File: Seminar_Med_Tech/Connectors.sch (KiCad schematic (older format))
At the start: 14 parts, among them J2 CONN_01X10, J3 CONN_02X10, J5 CONN_02X10

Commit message: update anno
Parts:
- gave numbers to parts that had none: 4
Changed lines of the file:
@@
 $EndComp
 $Comp
-L GND #PWR01
+L GND #PWR4
 U 1 1 593AE084
 P 7225 6000
-F 0 "#PWR01" H 7225 5750 50  0001 C CNN
+F 0 "#PWR4" H 7225 5750 50  0001 C CNN
 F 1 "GND" H 7225 5850 50  0000 C CNN
 F 2 "" H 7225 6000 50  0001 C CNN
@@
 $EndComp
 $Comp
-L GND #PWR02
+L GND #PWR2
 U 1 1 593AE114
 P 3675 5000
-F 0 "#PWR02" H 3675 4750 50  0001 C CNN
+F 0 "#PWR2" H 3675 4750 50  0001 C CNN
 F 1 "GND" H 3675 4850 50  0000 C CNN
 F 2 "" H 3675 5000 50  0001 C CNN
@@
 $EndComp
 $Comp
-L GND #PWR03
+L GND #PWR6
 U 1 1 593AE149
 P 9375 3700
-F 0 "#PWR03" H 9375 3450 50  0001 C CNN
+F 0 "#PWR6" H 9375 3450 50  0001 C CNN
 F 1 "GND" H 9375 3550 50  0000 C CNN
 F 2 "" H 9375 3700 50  0001 C CNN
@@
 SPI_CS2
 $Comp
-L GND #PWR04
+L GND #PWR5
 U 1 1 593E72B3
 P 9200 5600
-F 0 "#PWR04" H 9200 5350 50  0001 C CNN
+F 0 "#PWR5" H 9200 5350 50  0001 C CNN
 F 1 "GND" H 9200 5450 50  0000 C CNN
 F 2 "" H 9200 5600 50  0001 C CNN
@@
 $EndComp
 $Comp
-L GND #PWR05
+L GND #PWR3
 U 1 1 593E9316
 P 4700 4150
-F 0 "#PWR05" H 4700 3900 50  0001 C CNN
+F 0 "#PWR3" H 4700 3900 50  0001 C CNN
 F 1 "GND" H 4700 4000 50  0000 C CNN
 F 2 "" H 4700 4150 50  0001 C CNN
@@
 NoConn ~ 3850 6225
 $Comp
-L Jumper JP?
+L Jumper JP2
 U 1 1 5947B7A9
 P 1950 3550
-F 0 "JP?" H 1950 3700 50  0000 C CNN
+F 0 "JP2" H 1950 3700 50  0000 C CNN
 F 1 "Jumper" H 1950 3470 50  0000 C CNN
 F 2 "jumper:Jumper1x2" H 1950 3550 50  0001 C CNN
@@
 $EndComp
 $Comp
-L TEST_1P TP?
+L TEST_1P TP8
 U 1 1 5947B7AF
 P 1525 3550
-F 0 "TP?" H 1525 3820 50  0000 C CNN
+F 0 "TP8" H 1525 3820 50  0000 C CNN
 F 1 "TEST" H 1525 3750 50  0000 C CNN
 F 2 "Measurement_Points:Test_Point_Keystone_5000-5004_Miniature" H 1725 3550 50  0001 C CNN
@@
 $EndComp
 $Comp
-L C C?
+L C C33
 U 1 1 5947B7B5
 P 1300 3900
-F 0 "C?" H 1325 4000 50  0000 L CNN
+F 0 "C33" H 1325 4000 50  0000 L CNN
 F 1 "0.1uF" H 1325 3800 50  0000 L CNN
 F 2 "Capacitors_SMD:C_1206_HandSoldering" H 1338 3750 50  0001 C CNN
@@
 $EndComp
 $Comp
-L C C?
+L C C27
 U 1 1 5947B7BB
 P 925 3900
-F 0 "C?" H 950 4000 50  0000 L CNN
+F 0 "C27" H 950 4000 50  0000 L CNN
 F 1 "100uF" H 950 3800 50  0000 L CNN
 F 2 "Capacitors_SMD:C_1206_HandSoldering" H 963 3750 50  0001 C CNN
@@
 $EndComp
 $Comp
-L GND #PWR?
+L GND #PWR1
 U 1 1 5947B7C1
 P 1100 4150
-F 0 "#PWR?" H 1100 3900 50  0001 C CNN
+F 0 "#PWR1" H 1100 3900 50  0001 C CNN
 F 1 "GND" H 1100 4000 50  0000 C CNN
 F 2 "" H 1100 4150 50  0001 C CNN

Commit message: hi
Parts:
- TP7, TP8: footprint Measurement_Points:Test_Point_Keystone_5000-5004_Miniature -> Measurement_Points:Measurement_Point_Round-SMD-Pad_Small
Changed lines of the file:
@@
 $EndComp
 $Comp
-L GND #PWR4
+L GND #PWR01
 U 1 1 593AE084
 P 7225 6000
-F 0 "#PWR4" H 7225 5750 50  0001 C CNN
+F 0 "#PWR01" H 7225 5750 50  0001 C CNN
 F 1 "GND" H 7225 5850 50  0000 C CNN
 F 2 "" H 7225 6000 50  0001 C CNN
@@
 $EndComp
 $Comp
-L GND #PWR2
+L GND #PWR02
 U 1 1 593AE114
 P 3675 5000
-F 0 "#PWR2" H 3675 4750 50  0001 C CNN
+F 0 "#PWR02" H 3675 4750 50  0001 C CNN
 F 1 "GND" H 3675 4850 50  0000 C CNN
 F 2 "" H 3675 5000 50  0001 C CNN
@@
 $EndComp
 $Comp
-L GND #PWR6
+L GND #PWR03
 U 1 1 593AE149
 P 9375 3700
-F 0 "#PWR6" H 9375 3450 50  0001 C CNN
+F 0 "#PWR03" H 9375 3450 50  0001 C CNN
 F 1 "GND" H 9375 3550 50  0000 C CNN
 F 2 "" H 9375 3700 50  0001 C CNN
@@
 SPI_CS2
 $Comp
-L GND #PWR5
+L GND #PWR04
 U 1 1 593E72B3
 P 9200 5600
-F 0 "#PWR5" H 9200 5350 50  0001 C CNN
+F 0 "#PWR04" H 9200 5350 50  0001 C CNN
 F 1 "GND" H 9200 5450 50  0000 C CNN
 F 2 "" H 9200 5600 50  0001 C CNN
@@
 F 0 "TP7" H 4275 3820 50  0000 C CNN
 F 1 "TEST" H 4275 3750 50  0000 C CNN
-F 2 "Measurement_Points:Test_Point_Keystone_5000-5004_Miniature" H 4475 3550 50  0001 C CNN
+F 2 "Measurement_Points:Measurement_Point_Round-SMD-Pad_Small" H 4475 3550 50  0001 C CNN
 F 3 "" H 4475 3550 50  0001 C CNN
 	1    4275 3550
@@
 $EndComp
 $Comp
-L GND #PWR3
+L GND #PWR05
 U 1 1 593E9316
 P 4700 4150
-F 0 "#PWR3" H 4700 3900 50  0001 C CNN
+F 0 "#PWR05" H 4700 3900 50  0001 C CNN
 F 1 "GND" H 4700 4000 50  0000 C CNN
 F 2 "" H 4700 4150 50  0001 C CNN
@@
 F 0 "TP8" H 1525 3820 50  0000 C CNN
 F 1 "TEST" H 1525 3750 50  0000 C CNN
-F 2 "Measurement_Points:Test_Point_Keystone_5000-5004_Miniature" H 1725 3550 50  0001 C CNN
+F 2 "Measurement_Points:Measurement_Point_Round-SMD-Pad_Small" H 1725 3550 50  0001 C CNN
 F 3 "" H 1725 3550 50  0001 C CNN
 	1    1525 3550
@@
 $EndComp
 $Comp
-L GND #PWR1
+L GND #PWR06
 U 1 1 5947B7C1
 P 1100 4150
-F 0 "#PWR1" H 1100 3900 50  0001 C CNN
+F 0 "#PWR06" H 1100 3900 50  0001 C CNN
 F 1 "GND" H 1100 4000 50  0000 C CNN
 F 2 "" H 1100 4150 50  0001 C CNN

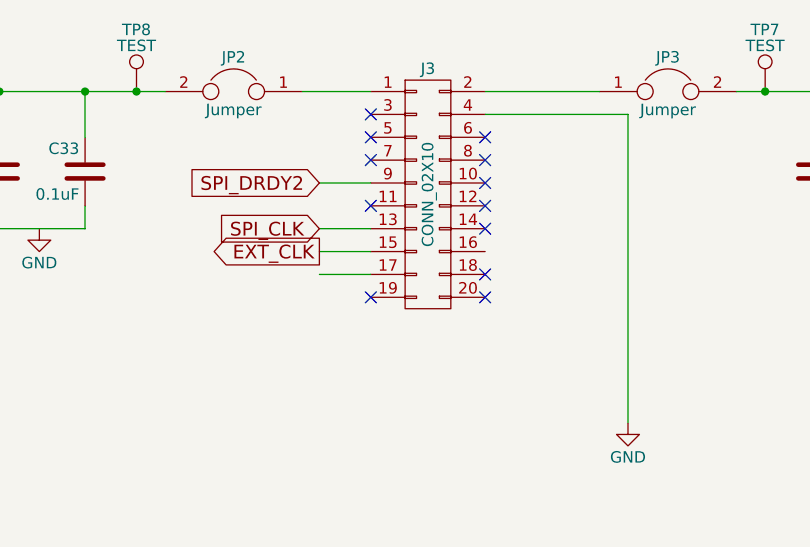
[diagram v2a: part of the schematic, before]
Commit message: Updated Connectors
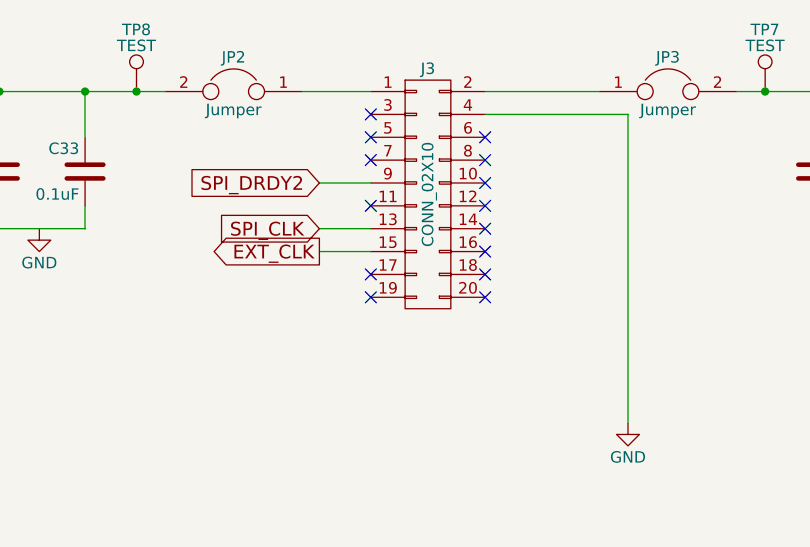
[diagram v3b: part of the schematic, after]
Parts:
- TP7, TP8: footprint Measurement_Points:Measurement_Point_Round-SMD-Pad_Small -> Measurement_Points:Test_Point_Keystone_5000-5004_Miniature
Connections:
- no-connect marks 17 -> 19
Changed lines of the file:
@@
 F 0 "TP7" H 4275 3820 50  0000 C CNN
 F 1 "TEST" H 4275 3750 50  0000 C CNN
-F 2 "Measurement_Points:Measurement_Point_Round-SMD-Pad_Small" H 4475 3550 50  0001 C CNN
+F 2 "Measurement_Points:Test_Point_Keystone_5000-5004_Miniature" H 4475 3550 50  0001 C CNN
 F 3 "" H 4475 3550 50  0001 C CNN
 	1    4275 3550
@@
 Wire Wire Line
 	2550 3950 2325 3950
-Wire Wire Line
-	2325 4350 2550 4350
 $Comp
 L CONN_01X10 J2
@@
 F 0 "TP8" H 1525 3820 50  0000 C CNN
 F 1 "TEST" H 1525 3750 50  0000 C CNN
-F 2 "Measurement_Points:Measurement_Point_Round-SMD-Pad_Small" H 1725 3550 50  0001 C CNN
+F 2 "Measurement_Points:Test_Point_Keystone_5000-5004_Miniature" H 1725 3550 50  0001 C CNN
 F 3 "" H 1725 3550 50  0001 C CNN
 	1    1525 3550
@@
 NoConn ~ 2550 3750
 NoConn ~ 2550 3850
+NoConn ~ 3050 4250
+NoConn ~ 2550 4350
 $EndSCHEMATC

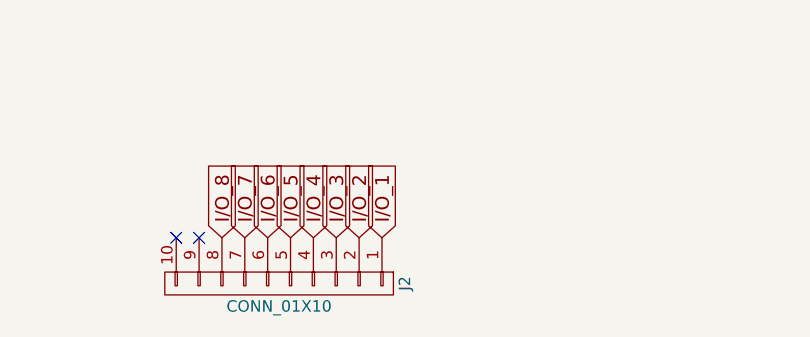
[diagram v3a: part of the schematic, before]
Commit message: Updated Schaltbild and changed BOM
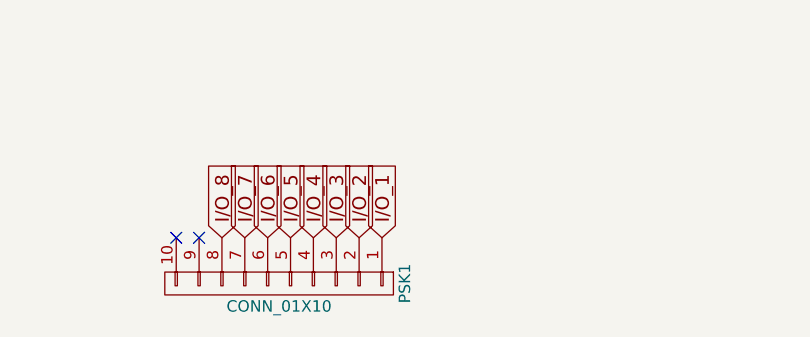
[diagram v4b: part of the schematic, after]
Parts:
- renumbered J2 to PSK1
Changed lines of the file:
@@
 	2550 3950 2325 3950
 $Comp
-L CONN_01X10 J2
+L CONN_01X10 PSK1
 U 1 1 5962D12A
 P 4200 6425
-F 0 "J2" H 4200 6975 50  0000 C CNN
+F 0 "PSK1" H 4200 6975 50  0000 C CNN
 F 1 "CONN_01X10" V 4300 6425 50  0000 C CNN
 F 2 "Pin_Headers:Pin_Header_Straight_1x10_Pitch2.54mm" H 4200 6425 50  0001 C CNN

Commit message: Updated Schaltbild and added LM317 footprint
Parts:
- JP2, JP3: footprint jumper:Jumper1x2 -> Jumper:Jumper1x2
- JP21: footprint jumper:jumper1x3 -> Jumper:jumper1x3
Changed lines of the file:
@@
 F 0 "JP21" H 7275 5650 50  0000 L CNN
 F 1 "Jumper_NC_Dual" H 7225 5850 50  0000 C BNN
-F 2 "jumper:jumper1x3" H 7225 5750 50  0001 C CNN
+F 2 "Jumper:jumper1x3" H 7225 5750 50  0001 C CNN
 F 3 "" H 7225 5750 50  0001 C CNN
 	1    7225 5750
@@
 F 0 "JP3" H 3850 3700 50  0000 C CNN
 F 1 "Jumper" H 3850 3470 50  0000 C CNN
-F 2 "jumper:Jumper1x2" H 3850 3550 50  0001 C CNN
+F 2 "Jumper:Jumper1x2" H 3850 3550 50  0001 C CNN
 F 3 "" H 3850 3550 50  0001 C CNN
 	1    3850 3550
@@
 F 0 "JP2" H 1950 3700 50  0000 C CNN
 F 1 "Jumper" H 1950 3470 50  0000 C CNN
-F 2 "jumper:Jumper1x2" H 1950 3550 50  0001 C CNN
+F 2 "Jumper:Jumper1x2" H 1950 3550 50  0001 C CNN
 F 3 "" H 1950 3550 50  0001 C CNN
 	1    1950 3550

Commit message: Updates Schaltbild
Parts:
- TP7, TP8: footprint Measurement_Points:Test_Point_Keystone_5000-5004_Miniature -> Measurement_Points:Measurement_Point_Round-TH_Small
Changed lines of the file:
@@
 F 0 "TP7" H 4275 3820 50  0000 C CNN
 F 1 "TEST" H 4275 3750 50  0000 C CNN
-F 2 "Measurement_Points:Test_Point_Keystone_5000-5004_Miniature" H 4475 3550 50  0001 C CNN
+F 2 "Measurement_Points:Measurement_Point_Round-TH_Small" H 4475 3550 50  0001 C CNN
 F 3 "" H 4475 3550 50  0001 C CNN
 	1    4275 3550
@@
 F 0 "TP8" H 1525 3820 50  0000 C CNN
 F 1 "TEST" H 1525 3750 50  0000 C CNN
-F 2 "Measurement_Points:Test_Point_Keystone_5000-5004_Miniature" H 1725 3550 50  0001 C CNN
+F 2 "Measurement_Points:Measurement_Point_Round-TH_Small" H 1725 3550 50  0001 C CNN
 F 3 "" H 1725 3550 50  0001 C CNN
 	1    1525 3550

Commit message: Update
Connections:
- net EXT_CLK: now also J5.20 (P20); no longer J3.15 (P15)
- net SPI_CS2: now also J3.15 (P15); no longer J5.20 (P20)
- net GPIO14: now reaches J5.16 (P16)
- net GPIO24: now reaches J5.18 (P18)
- net VCC_3.3V renamed 3.3V_Supply
- net VCC_5V renamed 5V_Supply
- no-connect marks 19 -> 17
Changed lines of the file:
@@
 Text GLabel 7025 3825 0    60   Input ~ 0
 SPI_CS1
-Text GLabel 2325 4250 0    60   Output ~ 0
+Text GLabel 8475 4425 2    60   Output ~ 0
 EXT_CLK
 $Comp
@@
 	1    0    0    -1
 $EndComp
-Text GLabel 8475 4425 2    60   Input ~ 0
+Text GLabel 2325 4250 0    60   Input ~ 0
 SPI_CS2
 $Comp
@@
 $EndComp
 Text GLabel 4875 3450 2    39   Input Italic 8
-VCC_5V
+5V_Supply
 Text GLabel 7600 5100 0    39   Input Italic 8
 DVDD
@@
 NoConn ~ 2550 3650
 NoConn ~ 7850 3925
-NoConn ~ 7850 4225
-NoConn ~ 7850 4325
 Connection ~ 4500 3550
 Connection ~ 4275 3550
@@
 $EndComp
 Text GLabel 925  3450 0    39   Input Italic 8
-VCC_3.3V
+3.3V_Supply
 Wire Wire Line
 	1650 3550 925  3550
@@
 NoConn ~ 3050 4250
 NoConn ~ 2550 4350
+Text GLabel 8475 4225 2    60   Input ~ 0
+GPIO14
+Text GLabel 8475 4325 2    60   Input ~ 0
+GPIO24
+Wire Wire Line
+	8475 4225 7850 4225
+Wire Wire Line
+	7850 4325 8475 4325
 $EndSCHEMATC

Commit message: Update
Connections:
- net I/O_1: now also J5.4 (P4); no longer J5.9 (P9)
- net I/O_2: now also J5.6 (P6); no longer J5.11 (P11)
- net I/O_3: now also J5.8 (P8); no longer J5.13 (P13)
- net I/O_4: now also J5.9 (P9); no longer J5.15 (P15)
- net I/O_5: now also J5.11 (P11); no longer J5.17 (P17)
- net I/O_6: now also J5.13 (P13); no longer J5.4 (P4)
- net I/O_7: now also J5.15 (P15); no longer J5.6 (P6)
- net I/O_8: now also J5.17 (P17); no longer J5.8 (P8)
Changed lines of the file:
@@
 Text GLabel 9850 5775 2    39   Input Italic 8
 AGND
+Text GLabel 7025 4125 0    60   Input ~ 0
+I/O_6
+Text GLabel 7025 4225 0    60   Input ~ 0
+I/O_7
+Text GLabel 7025 4325 0    60   Input ~ 0
+I/O_8
 Text GLabel 7025 3925 0    60   Input ~ 0
-I/O_1
+I/O_4
 Text GLabel 7025 4025 0    60   Input ~ 0
-I/O_2
-Text GLabel 7025 4125 0    60   Input ~ 0
-I/O_3
-Text GLabel 7025 4225 0    60   Input ~ 0
-I/O_4
-Text GLabel 7025 4325 0    60   Input ~ 0
 I/O_5
 Text GLabel 8475 3825 2    60   Input ~ 0
-I/O_8
+I/O_3
 Text GLabel 8475 3725 2    60   Input ~ 0
-I/O_7
+I/O_2
 Text GLabel 8475 3625 2    60   Input ~ 0
-I/O_6
+I/O_1
 Wire Wire Line
 	2550 4150 2325 4150
